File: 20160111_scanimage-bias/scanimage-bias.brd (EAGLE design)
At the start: 65 x 40 mm, 0 parts

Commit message: Made libraries
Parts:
- added C1: 1u, SparkFun-Capacitors:1206
- added J1: (no value), SparkFun-Connectors:1X03
- added R1: 10k, SparkFun-Resistors:1206
- added U$1: AD780, kimth:SOIC-8
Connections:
- new net GND: C1.1, J1.2, U$1.P$2, U$1.P$6
- new net VCC: J1.1
- new net VNEG: C1.2, J1.3, R1.1
- new net VREF: R1.2, U$1.P$4
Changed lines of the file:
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@@
 <layer number="48" name="Document" color="7" fill="1" visible="yes" active="yes"/>
 <layer number="49" name="Reference" color="7" fill="1" visible="yes" active="yes"/>
+<layer number="50" name="dxf" color="7" fill="1" visible="no" active="no"/>
 <layer number="51" name="tDocu" color="7" fill="1" visible="yes" active="yes"/>
 <layer number="52" name="bDocu" color="7" fill="1" visible="yes" active="yes"/>
+<layer number="53" name="tGND_GNDA" color="7" fill="9" visible="no" active="no"/>
+<layer number="54" name="bGND_GNDA" color="1" fill="9" visible="no" active="no"/>
+<layer number="56" name="wert" color="7" fill="1" visible="no" active="no"/>
+<layer number="57" name="tCAD" color="7" fill="1" visible="no" active="no"/>
+<layer number="59" name="tCarbon" color="7" fill="1" visible="no" active="no"/>
+<layer number="60" name="bCarbon" color="7" fill="1" visible="no" active="no"/>
 <layer number="90" name="Modules" color="5" fill="1" visible="no" active="no"/>
 <layer number="91" name="Nets" color="2" fill="1" visible="no" active="no"/>
@@
 <layer number="97" name="Info" color="7" fill="1" visible="no" active="no"/>
 <layer number="98" name="Guide" color="6" fill="1" visible="no" active="no"/>
+<layer number="99" name="SpiceOrder" color="7" fill="1" visible="no" active="no"/>
+<layer number="100" name="Muster" color="7" fill="1" visible="no" active="no"/>
+<layer number="101" name="Patch_Top" color="12" fill="4" visible="yes" active="yes"/>
+<layer number="102" name="Vscore" color="7" fill="1" visible="yes" active="yes"/>
+<layer number="103" name="tMap" color="7" fill="1" visible="yes" active="yes"/>
+<layer number="104" name="Name" color="16" fill="1" visible="yes" active="yes"/>
+<layer number="105" name="tPlate" color="7" fill="1" visible="yes" active="yes"/>
+<layer number="106" name="bPlate" color="7" fill="1" visible="yes" active="yes"/>
+<layer number="107" name="Crop" color="7" fill="1" visible="yes" active="yes"/>
+<layer number="108" name="tplace-old" color="10" fill="1" visible="yes" active="yes"/>
+<layer number="109" name="ref-old" color="11" fill="1" visible="yes" active="yes"/>
+<layer number="110" name="fp0" color="7" fill="1" visible="yes" active="yes"/>
+<layer number="111" name="LPC17xx" color="7" fill="1" visible="yes" active="yes"/>
+<layer number="112" name="tSilk" color="7" fill="1" visible="yes" active="yes"/>
+<layer number="113" name="IDFDebug" color="4" fill="1" visible="yes" active="yes"/>
+<layer number="114" name="Badge_Outline" color="7" fill="1" visible="yes" active="yes"/>
+<layer number="115" name="ReferenceISLANDS" color="7" fill="1" visible="yes" active="yes"/>
+<layer number="116" name="Patch_BOT" color="9" fill="4" visible="yes" active="yes"/>
+<layer number="118" name="Rect_Pads" color="7" fill="1" visible="yes" active="yes"/>
+<layer number="121" name="_tsilk" color="7" fill="1" visible="yes" active="yes"/>
+<layer number="122" name="_bsilk" color="7" fill="1" visible="yes" active="yes"/>
+<layer number="123" name="tTestmark" color="7" fill="1" visible="yes" active="yes"/>
+<layer number="124" name="bTestmark" color="7" fill="1" visible="yes" active="yes"/>
+<layer number="125" name="_tNames" color="7" fill="1" visible="yes" active="yes"/>
+<layer number="126" name="_bNames" color="7" fill="1" visible="yes" active="yes"/>
+<layer number="127" name="_tValues" color="7" fill="1" visible="yes" active="yes"/>
+<layer number="128" name="_bValues" color="7" fill="1" visible="yes" active="yes"/>
+<layer number="129" name="Mask" color="7" fill="1" visible="yes" active="yes"/>
+<layer number="131" name="tAdjust" color="7" fill="1" visible="yes" active="yes"/>
+<layer number="132" name="bAdjust" color="7" fill="1" visible="yes" active="yes"/>
+<layer number="144" name="Drill_legend" color="7" fill="1" visible="yes" active="yes"/>
+<layer number="150" name="Notes" color="7" fill="1" visible="yes" active="yes"/>
+<layer number="151" name="HeatSink" color="7" fill="1" visible="yes" active="yes"/>
+<layer number="152" name="_bDocu" color="7" fill="1" visible="yes" active="yes"/>
+<layer number="153" name="FabDoc1" color="7" fill="1" visible="yes" active="yes"/>
+<layer number="154" name="FabDoc2" color="7" fill="1" visible="yes" active="yes"/>
+<layer number="155" name="FabDoc3" color="7" fill="1" visible="yes" active="yes"/>
+<layer number="199" name="Contour" color="7" fill="1" visible="yes" active="yes"/>
+<layer number="200" name="200bmp" color="1" fill="10" visible="yes" active="yes"/>
+<layer number="201" name="201bmp" color="2" fill="10" visible="yes" active="yes"/>
+<layer number="202" name="202bmp" color="3" fill="10" visible="yes" active="yes"/>
+<layer number="203" name="203bmp" color="4" fill="10" visible="yes" active="yes"/>
+<layer number="204" name="204bmp" color="5" fill="10" visible="yes" active="yes"/>
+<layer number="205" name="205bmp" color="6" fill="10" visible="yes" active="yes"/>
+<layer number="206" name="206bmp" color="7" fill="10" visible="yes" active="yes"/>
+<layer number="207" name="207bmp" color="8" fill="10" visible="yes" active="yes"/>
+<layer number="208" name="208bmp" color="9" fill="10" visible="yes" active="yes"/>
+<layer number="209" name="209bmp" color="7" fill="1" visible="yes" active="yes"/>
+<layer number="210" name="210bmp" color="7" fill="1" visible="yes" active="yes"/>
+<layer number="211" name="211bmp" color="7" fill="1" visible="yes" active="yes"/>
+<layer number="212" name="212bmp" color="7" fill="1" visible="yes" active="yes"/>
+<layer number="213" name="213bmp" color="7" fill="1" visible="yes" active="yes"/>
+<layer number="214" name="214bmp" color="7" fill="1" visible="yes" active="yes"/>
+<layer number="215" name="215bmp" color="7" fill="1" visible="yes" active="yes"/>
+<layer number="216" name="216bmp" color="7" fill="1" visible="yes" active="yes"/>
+<layer number="217" name="217bmp" color="18" fill="1" visible="no" active="no"/>
+<layer number="218" name="218bmp" color="19" fill="1" visible="no" active="no"/>
+<layer number="219" name="219bmp" color="20" fill="1" visible="no" active="no"/>
+<layer number="220" name="220bmp" color="21" fill="1" visible="no" active="no"/>
+<layer number="221" name="221bmp" color="22" fill="1" visible="no" active="no"/>
+<layer number="222" name="222bmp" color="23" fill="1" visible="no" active="no"/>
+<layer number="223" name="223bmp" color="24" fill="1" visible="no" active="no"/>
+<layer number="224" name="224bmp" color="25" fill="1" visible="no" active="no"/>
+<layer number="225" name="225bmp" color="7" fill="1" visible="yes" active="yes"/>
+<layer number="226" name="226bmp" color="7" fill="1" visible="yes" active="yes"/>
+<layer number="227" name="227bmp" color="7" fill="1" visible="yes" active="yes"/>
+<layer number="228" name="228bmp" color="7" fill="1" visible="yes" active="yes"/>
+<layer number="229" name="229bmp" color="7" fill="1" visible="yes" active="yes"/>
+<layer number="230" name="230bmp" color="7" fill="1" visible="yes" active="yes"/>
+<layer number="231" name="231bmp" color="7" fill="1" visible="yes" active="yes"/>
+<layer number="248" name="Housing" color="7" fill="1" visible="yes" active="yes"/>
+<layer number="249" name="Edge" color="7" fill="1" visible="yes" active="yes"/>
+<layer number="250" name="Descript" color="3" fill="1" visible="no" active="no"/>
+<layer number="251" name="SMDround" color="12" fill="11" visible="no" active="no"/>
+<layer number="254" name="cooling" color="7" fill="1" visible="yes" active="yes"/>
+<layer number="255" name="routoute" color="7" fill="1" visible="yes" active="yes"/>
 </layers>
 <board>
@@
 </autorouter>
 <elements>
+<element name="U$1" library="kimth" package="SOIC-8" value="AD780" x="11" y="7"/>
+<element name="R1" library="SparkFun-Resistors" package="1206" value="10k" x="3" y="-2"/>
+<element name="C1" library="SparkFun-Capacitors" package="1206" value="1u" x="3" y="-5"/>
+<element name="J1" library="SparkFun-Connectors" package="1X03" value="" x="2" y="-10"/>
 </elements>
 <signals>
+<signal name="GND">
+<contactref element="U$1" pad="P$6"/>
+<contactref element="U$1" pad="P$2"/>
+<contactref element="C1" pad="1"/>
+<contactref element="J1" pad="2"/>
+<wire x1="8.4" y1="7.635" x2="13.6" y2="6.365" width="0" layer="19" extent="1-1"/>
+<wire x1="1.6" y1="-5" x2="8.4" y2="7.635" width="0" layer="19" extent="1-1"/>
+<wire x1="4.54" y1="-10" x2="1.6" y2="-5" width="0" layer="19" extent="1-1"/>
+</signal>
+<signal name="VREF">
+<contactref element="U$1" pad="P$4"/>
+<contactref element="R1" pad="2"/>
+<wire x1="4.4" y1="-2" x2="8.4" y2="5.095" width="0" layer="19" extent="1-1"/>
+</signal>
+<signal name="VNEG">
+<contactref element="R1" pad="1"/>
+<contactref element="C1" pad="2"/>
+<contactref element="J1" pad="3"/>
+<wire x1="4.4" y1="-5" x2="7.08" y2="-10" width="0" layer="19" extent="1-1"/>
+<wire x1="1.6" y1="-2" x2="4.4" y2="-5" width="0" layer="19" extent="1-1"/>
+</signal>
+<signal name="VCC">
+<contactref element="J1" pad="1"/>
+</signal>
 </signals>
 </board>

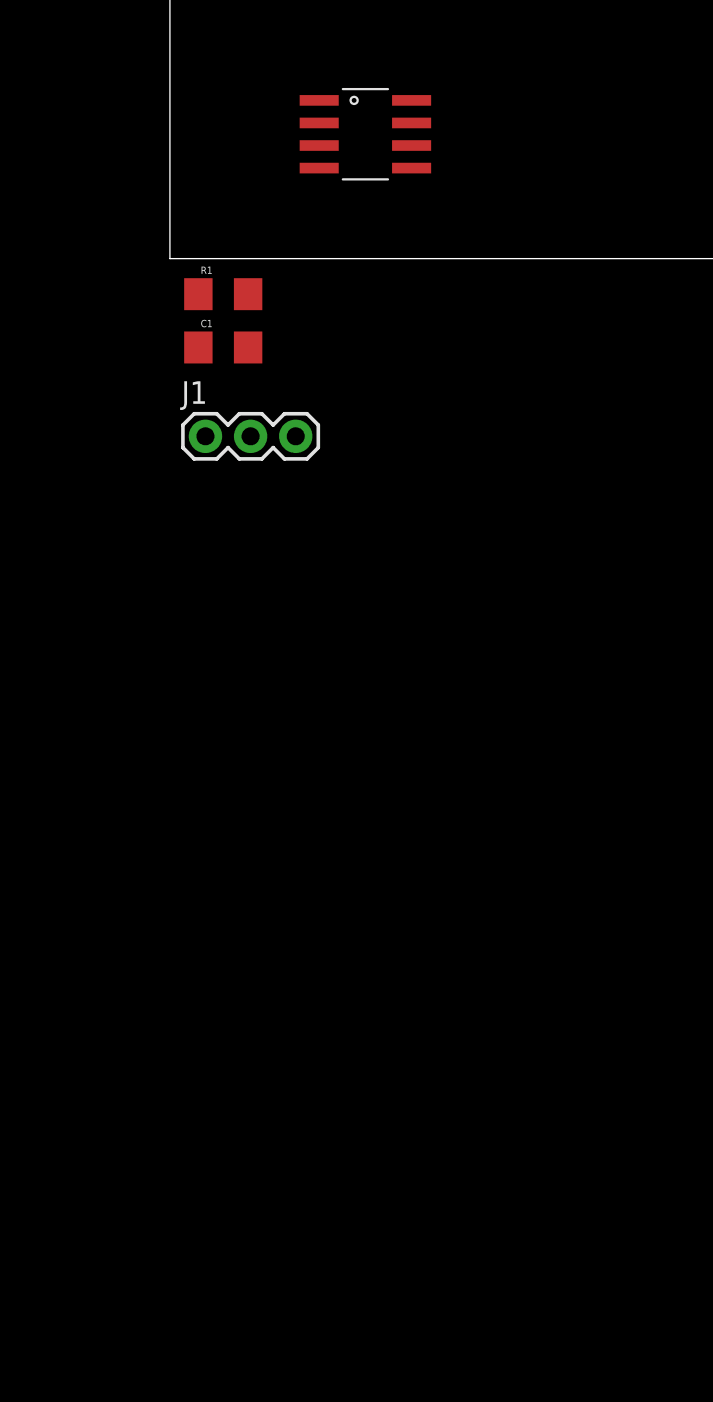
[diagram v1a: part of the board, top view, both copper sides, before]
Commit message: Finish schematic
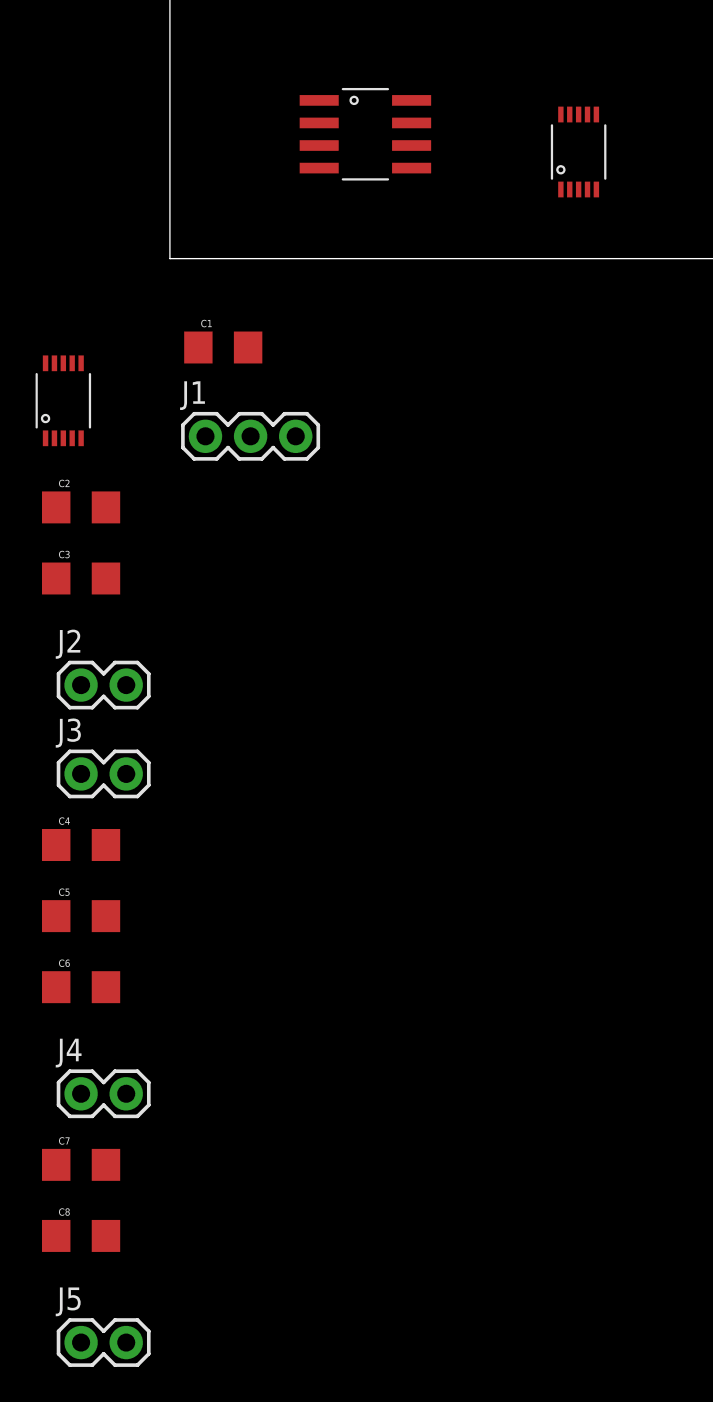
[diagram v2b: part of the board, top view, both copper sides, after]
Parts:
- removed R1: 10k, SparkFun-Resistors:1206
- added C2, C3, C4, C7, C8: 0.1u, SparkFun-Capacitors:1206
- added C5, C6: 10u, SparkFun-Capacitors:1206
- added J2, J3, J4, J5: (no value), SparkFun-Connectors:1X02
- added U$2, U$3: AD8250, kimth:MSOP-10
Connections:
- new net IN1: J2.1, U$2.P$10
- new net IN2: J4.1, U$3.P$10
- new net OUT1: J3.2, U$2.P$7
- new net OUT2: J5.2, U$3.P$7
- net GND: now also C1.2, C2.2, C3.1, C4.2, C5.2, C6.1, C7.2, C8.1, J2.2, J3.1, J4.2, J5.1, U$1.P$4, U$2.P$1, U$2.P$2, U$2.P$4, U$2.P$5, U$3.P$1, U$3.P$2, U$3.P$4, U$3.P$5; no longer C1.1, U$1.P$2, U$1.P$6
- net VCC: now also C1.1, C2.1, C5.1, C7.1, U$1.P$2, U$2.P$8, U$3.P$8
- net VNEG: now also C3.2, C6.2, C8.2, U$2.P$3, U$2.P$6, U$3.P$3, U$3.P$6; no longer C1.2, R1.1
- net VREF: now also C4.1, U$1.P$6, U$2.P$9, U$3.P$9; no longer R1.2, U$1.P$4
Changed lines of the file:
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@@
 <elements>
 <element name="U$1" library="kimth" package="SOIC-8" value="AD780" x="11" y="7"/>
-<element name="R1" library="SparkFun-Resistors" package="1206" value="10k" x="3" y="-2"/>
 <element name="C1" library="SparkFun-Capacitors" package="1206" value="1u" x="3" y="-5"/>
 <element name="J1" library="SparkFun-Connectors" package="1X03" value="" x="2" y="-10"/>
+<element name="U$2" library="kimth" package="MSOP-10" value="AD8250" x="23" y="6"/>
+<element name="U$3" library="kimth" package="MSOP-10" value="AD8250" x="-6" y="-8"/>
+<element name="C2" library="SparkFun-Capacitors" package="1206" value="0.1u" x="-5" y="-14"/>
+<element name="C3" library="SparkFun-Capacitors" package="1206" value="0.1u" x="-5" y="-18"/>
+<element name="J2" library="SparkFun-Connectors" package="1X02" value="" x="-5" y="-24"/>
+<element name="J3" library="SparkFun-Connectors" package="1X02" value="" x="-5" y="-29"/>
+<element name="C4" library="SparkFun-Capacitors" package="1206" value="0.1u" x="-5" y="-33"/>
+<element name="C5" library="SparkFun-Capacitors" package="1206" value="10u" x="-5" y="-37"/>
+<element name="C6" library="SparkFun-Capacitors" package="1206" value="10u" x="-5" y="-41"/>
+<element name="J4" library="SparkFun-Connectors" package="1X02" value="" x="-5" y="-47"/>
+<element name="C7" library="SparkFun-Capacitors" package="1206" value="0.1u" x="-5" y="-51"/>
+<element name="C8" library="SparkFun-Capacitors" package="1206" value="0.1u" x="-5" y="-55"/>
+<element name="J5" library="SparkFun-Connectors" package="1X02" value="" x="-5" y="-61"/>
 </elements>
 <signals>
 <signal name="GND">
-<contactref element="U$1" pad="P$6"/>
-<contactref element="U$1" pad="P$2"/>
-<contactref element="C1" pad="1"/>
 <contactref element="J1" pad="2"/>
-<wire x1="8.4" y1="7.635" x2="13.6" y2="6.365" width="0" layer="19" extent="1-1"/>
-<wire x1="1.6" y1="-5" x2="8.4" y2="7.635" width="0" layer="19" extent="1-1"/>
-<wire x1="4.54" y1="-10" x2="1.6" y2="-5" width="0" layer="19" extent="1-1"/>
+<contactref element="U$2" pad="P$2"/>
+<contactref element="U$2" pad="P$5"/>
+<contactref element="U$2" pad="P$4"/>
+<contactref element="C2" pad="2"/>
+<contactref element="C3" pad="1"/>
+<contactref element="J2" pad="2"/>
+<contactref element="U$2" pad="P$1"/>
+<contactref element="J3" pad="1"/>
+<contactref element="C1" pad="2"/>
+<contactref element="U$1" pad="P$4"/>
+<contactref element="C4" pad="2"/>
+<contactref element="C5" pad="2"/>
+<contactref element="C6" pad="1"/>
+<contactref element="J4" pad="2"/>
+<contactref element="U$3" pad="P$1"/>
+<contactref element="U$3" pad="P$2"/>
+<contactref element="U$3" pad="P$5"/>
+<contactref element="U$3" pad="P$4"/>
+<contactref element="C7" pad="2"/>
+<contactref element="C8" pad="1"/>
+<contactref element="J5" pad="1"/>
+<wire x1="-6.4" y1="-55" x2="-5" y2="-61" width="0" layer="19" extent="1-1"/>
+<wire x1="-3.6" y1="-51" x2="-6.4" y2="-55" width="0" layer="19" extent="1-1"/>
+<wire x1="-2.46" y1="-47" x2="-3.6" y2="-51" width="0" layer="19" extent="1-1"/>
+<wire x1="-6.4" y1="-41" x2="-2.46" y2="-47" width="0" layer="19" extent="1-1"/>
+<wire x1="-3.6" y1="-37" x2="-6.4" y2="-41" width="0" layer="19" extent="1-1"/>
+<wire x1="-3.6" y1="-33" x2="-3.6" y2="-37" width="0" layer="19" extent="1-1"/>
+<wire x1="-5" y1="-29" x2="-3.6" y2="-33" width="0" layer="19" extent="1-1"/>
+<wire x1="-2.46" y1="-24" x2="-5" y2="-29" width="0" layer="19" extent="1-1"/>
+<wire x1="-6.4" y1="-18" x2="-2.46" y2="-24" width="0" layer="19" extent="1-1"/>
+<wire x1="-3.6" y1="-14" x2="-6.4" y2="-18" width="0" layer="19" extent="1-1"/>
+<wire x1="-5" y1="-10.11" x2="-3.6" y2="-14" width="0" layer="19" extent="1-1"/>
+<wire x1="-5.5" y1="-10.11" x2="-5" y2="-10.11" width="0" layer="19" extent="1-1"/>
+<wire x1="-6.5" y1="-10.11" x2="-5.5" y2="-10.11" width="0" layer="19" extent="1-1"/>
+<wire x1="-7" y1="-10.11" x2="-6.5" y2="-10.11" width="0" layer="19" extent="1-1"/>
+<wire x1="4.54" y1="-10" x2="-3.6" y2="-14" width="0" layer="19" extent="1-1"/>
+<wire x1="4.4" y1="-5" x2="4.54" y2="-10" width="0" layer="19" extent="1-1"/>
+<wire x1="8.4" y1="5.095" x2="4.4" y2="-5" width="0" layer="19" extent="1-1"/>
+<wire x1="22" y1="3.89" x2="8.4" y2="5.095" width="0" layer="19" extent="1-1"/>
+<wire x1="22.5" y1="3.89" x2="22" y2="3.89" width="0" layer="19" extent="1-1"/>
+<wire x1="23.5" y1="3.89" x2="22.5" y2="3.89" width="0" layer="19" extent="1-1"/>
+<wire x1="24" y1="3.89" x2="23.5" y2="3.89" width="0" layer="19" extent="1-1"/>
 </signal>
 <signal name="VREF">
-<contactref element="U$1" pad="P$4"/>
-<contactref element="R1" pad="2"/>
-<wire x1="4.4" y1="-2" x2="8.4" y2="5.095" width="0" layer="19" extent="1-1"/>
+<contactref element="U$2" pad="P$9"/>
+<contactref element="U$1" pad="P$6"/>
+<contactref element="C4" pad="1"/>
+<contactref element="U$3" pad="P$9"/>
+<wire x1="-6.5" y1="-5.89" x2="-6.4" y2="-33" width="0" layer="19" extent="1-1"/>
+<wire x1="13.6" y1="6.365" x2="-6.5" y2="-5.89" width="0" layer="19" extent="1-1"/>
+<wire x1="22.5" y1="8.11" x2="13.6" y2="6.365" width="0" layer="19" extent="1-1"/>
 </signal>
 <signal name="VNEG">
-<contactref element="R1" pad="1"/>
-<contactref element="C1" pad="2"/>
 <contactref element="J1" pad="3"/>
-<wire x1="4.4" y1="-5" x2="7.08" y2="-10" width="0" layer="19" extent="1-1"/>
-<wire x1="1.6" y1="-2" x2="4.4" y2="-5" width="0" layer="19" extent="1-1"/>
+<contactref element="U$2" pad="P$3"/>
+<contactref element="U$2" pad="P$6"/>
+<contactref element="C3" pad="2"/>
+<contactref element="C6" pad="2"/>
+<contactref element="U$3" pad="P$3"/>
+<contactref element="U$3" pad="P$6"/>
+<contactref element="C8" pad="2"/>
+<wire x1="-3.6" y1="-41" x2="-3.6" y2="-55" width="0" layer="19" extent="1-1"/>
+<wire x1="-3.6" y1="-18" x2="-3.6" y2="-41" width="0" layer="19" extent="1-1"/>
+<wire x1="-6" y1="-10.11" x2="-3.6" y2="-18" width="0" layer="19" extent="1-1"/>
+<wire x1="-5" y1="-5.89" x2="-6" y2="-10.11" width="0" layer="19" extent="1-1"/>
+<wire x1="7.08" y1="-10" x2="-5" y2="-5.89" width="0" layer="19" extent="1-1"/>
+<wire x1="23" y1="3.89" x2="7.08" y2="-10" width="0" layer="19" extent="1-1"/>
+<wire x1="24" y1="8.11" x2="23" y2="3.89" width="0" layer="19" extent="1-1"/>
 </signal>
 <signal name="VCC">
 <contactref element="J1" pad="1"/>
+<contactref element="U$2" pad="P$8"/>
+<contactref element="C2" pad="1"/>
+<contactref element="C1" pad="1"/>
+<contactref element="U$1" pad="P$2"/>
+<contactref element="C5" pad="1"/>
+<contactref element="U$3" pad="P$8"/>
+<contactref element="C7" pad="1"/>
+<wire x1="-6.4" y1="-37" x2="-6.4" y2="-51" width="0" layer="19" extent="1-1"/>
+<wire x1="-6.4" y1="-14" x2="-6.4" y2="-37" width="0" layer="19" extent="1-1"/>
+<wire x1="-6" y1="-5.89" x2="-6.4" y2="-14" width="0" layer="19" extent="1-1"/>
+<wire x1="1.6" y1="-5" x2="-6" y2="-5.89" width="0" layer="19" extent="1-1"/>
+<wire x1="2" y1="-10" x2="1.6" y2="-5" width="0" layer="19" extent="1-1"/>
+<wire x1="8.4" y1="7.635" x2="1.6" y2="-5" width="0" layer="19" extent="1-1"/>
+<wire x1="23" y1="8.11" x2="8.4" y2="7.635" width="0" layer="19" extent="1-1"/>
+</signal>
+<signal name="IN1">
+<contactref element="J2" pad="1"/>
+<contactref element="U$2" pad="P$10"/>
+<wire x1="-5" y1="-24" x2="22" y2="8.11" width="0" layer="19" extent="1-1"/>
+</signal>
+<signal name="OUT1">
+<contactref element="U$2" pad="P$7"/>
+<contactref element="J3" pad="2"/>
+<wire x1="-2.46" y1="-29" x2="23.5" y2="8.11" width="0" layer="19" extent="1-1"/>
+</signal>
+<signal name="IN2">
+<contactref element="J4" pad="1"/>
+<contactref element="U$3" pad="P$10"/>
+<wire x1="-7" y1="-5.89" x2="-5" y2="-47" width="0" layer="19" extent="1-1"/>
+</signal>
+<signal name="OUT2">
+<contactref element="U$3" pad="P$7"/>
+<contactref element="J5" pad="2"/>
+<wire x1="-5.5" y1="-5.89" x2="-2.46" y2="-61" width="0" layer="19" extent="1-1"/>
 </signal>
 </signals>
